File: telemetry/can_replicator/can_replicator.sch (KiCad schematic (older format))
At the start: 25 parts, among them J1 CONN_02X03, U1 MCP2561-E_SN, U2 ATMEGA16M1, Y1 Crystal_SMD

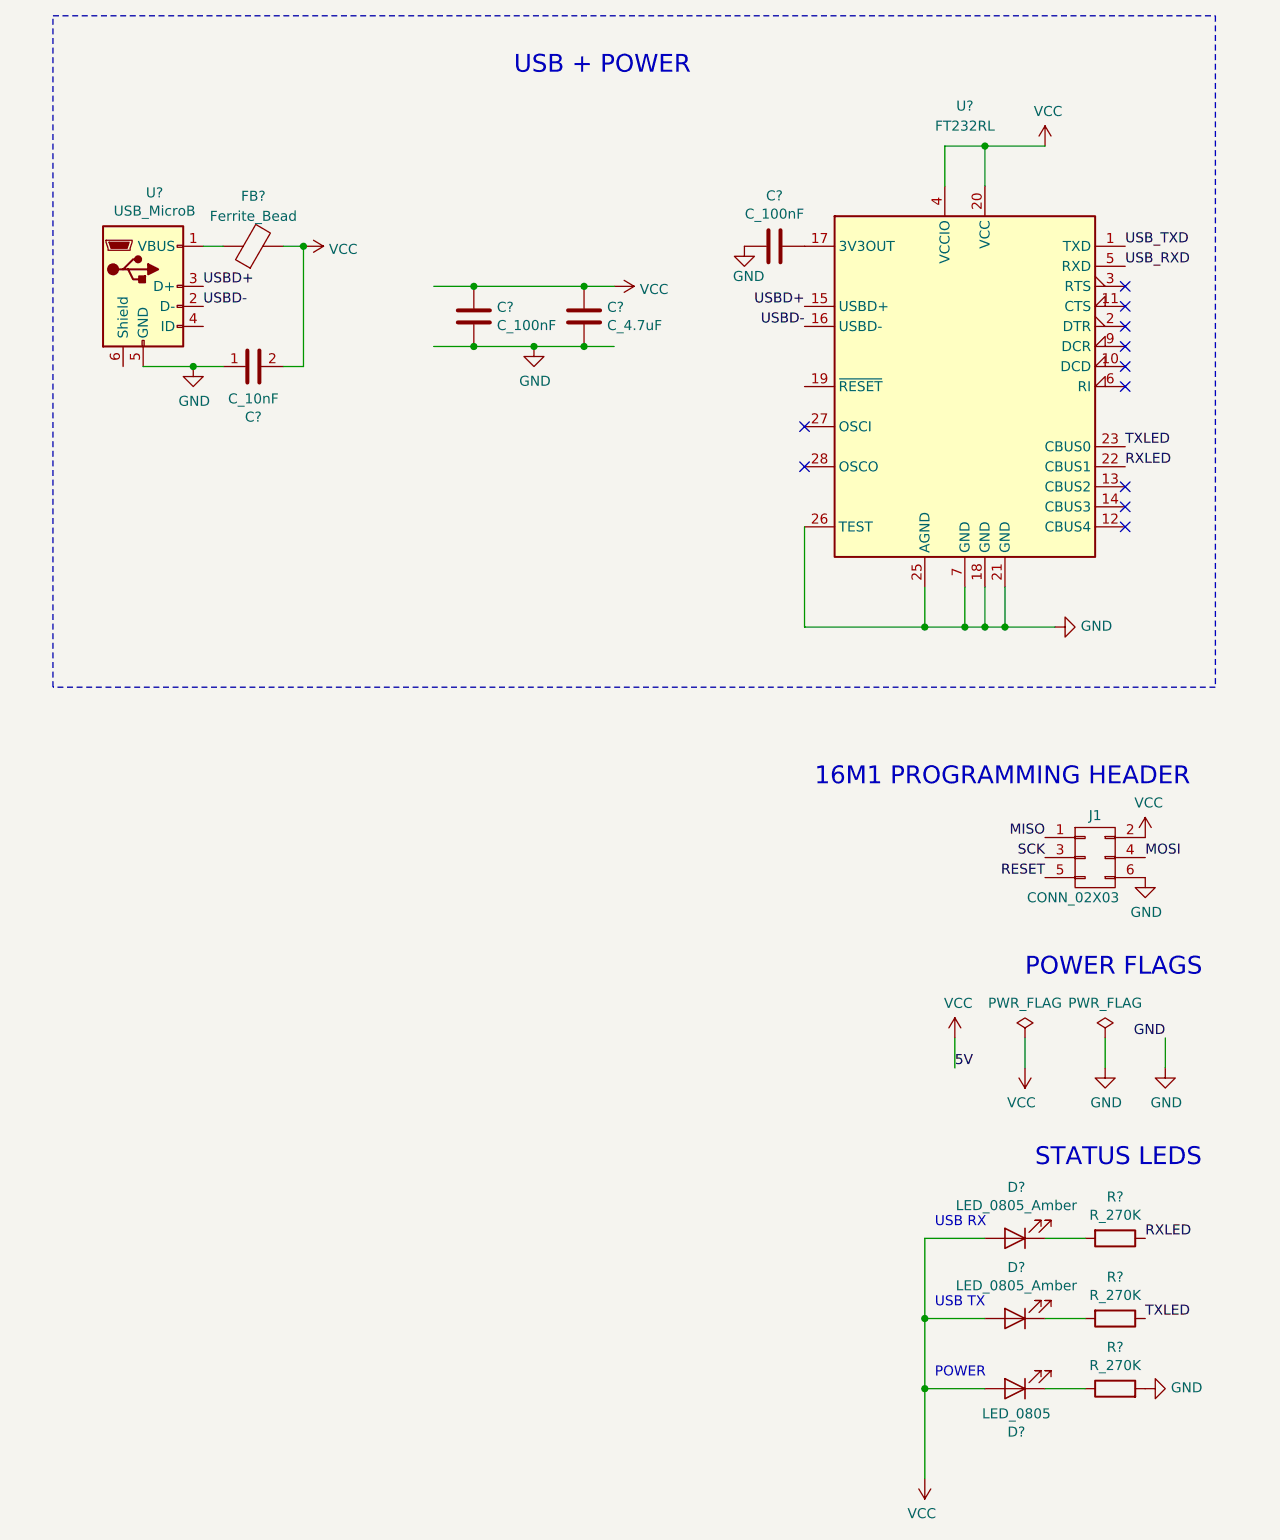
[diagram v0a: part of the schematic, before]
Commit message: fix: GND down, VCC up
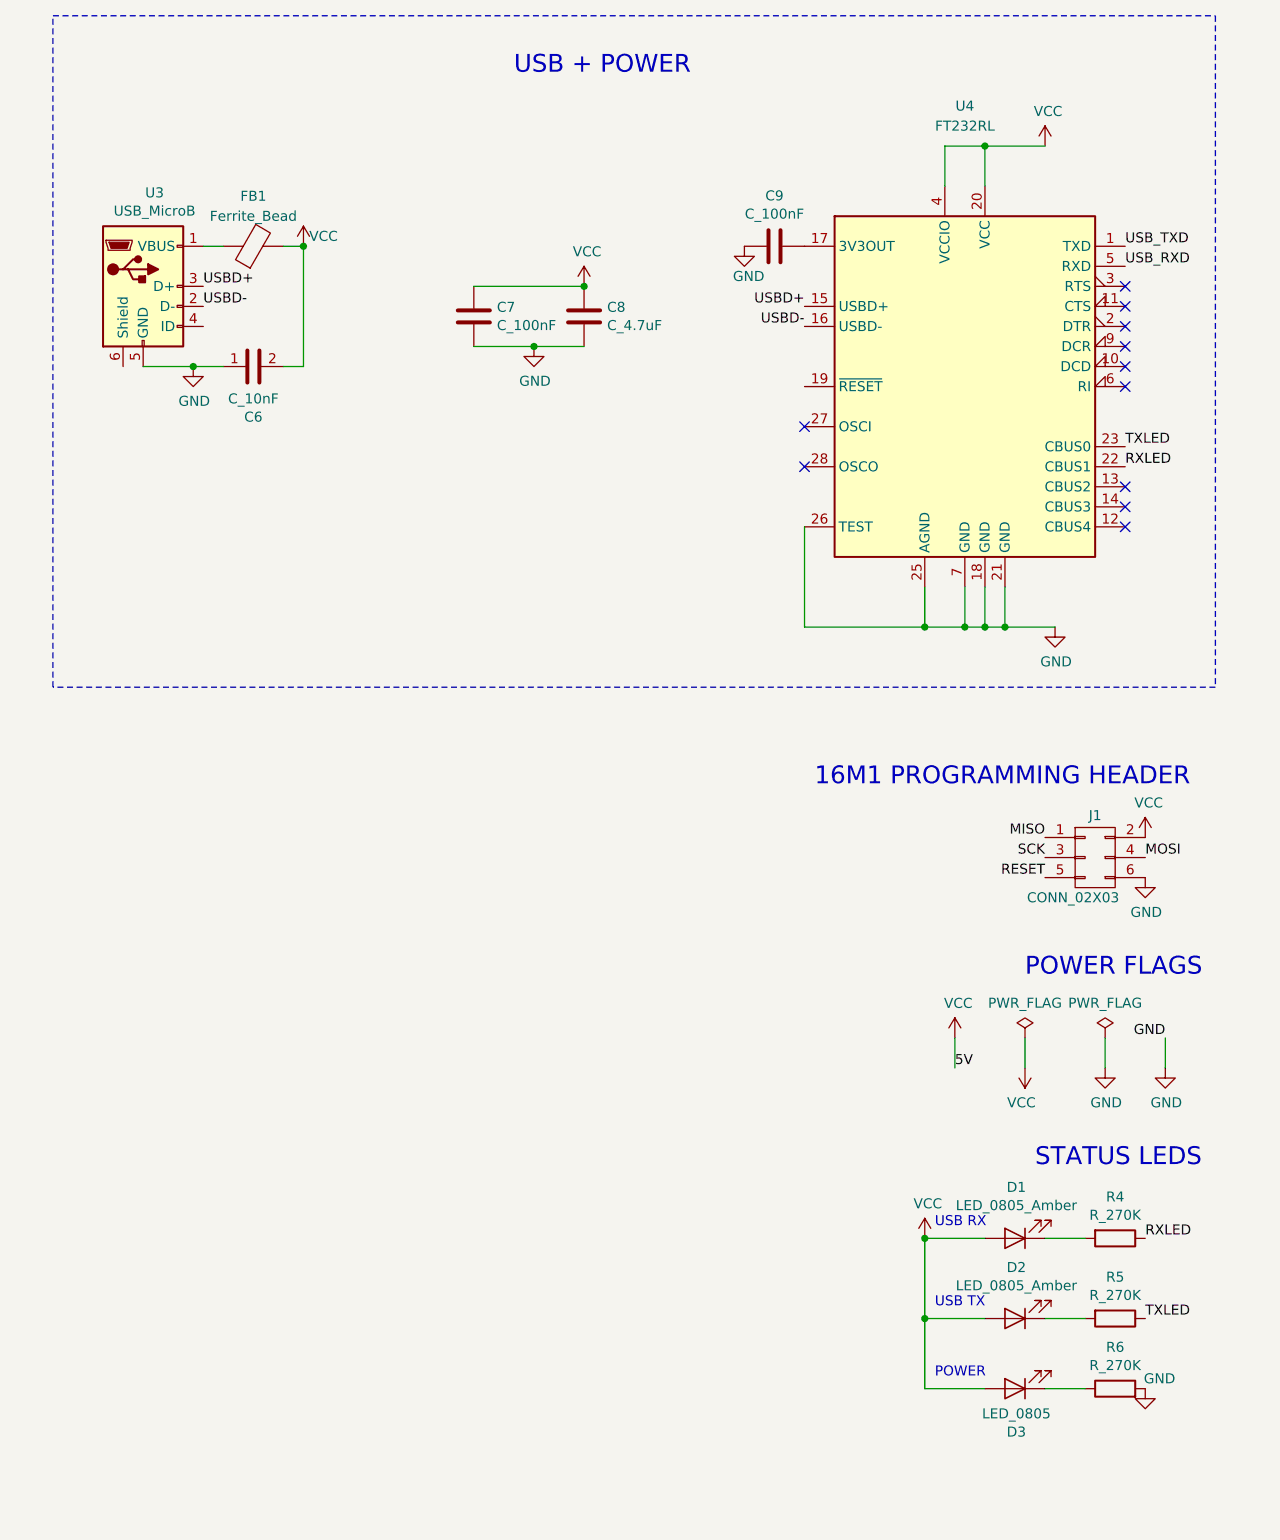
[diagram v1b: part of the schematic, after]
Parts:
- gave numbers to parts that had none: 13
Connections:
- wire segments 73 -> 68
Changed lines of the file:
@@
 Connection ~ 14800 3700
 $Comp
-L power:GND #PWR0101
-U 1 1 5FABE223
-P 15450 3700
-F 0 "#PWR0101" H 15450 3450 50  0001 C CNN
-F 1 "GND" V 15455 3572 50  0000 R CNN
-F 2 "" H 15450 3700 50  0001 C CNN
-F 3 "" H 15450 3700 50  0001 C CNN
-	1    15450 3700
-	0    -1   -1   0
-$EndComp
-$Comp
-L formula:FT232RL U?
+L formula:FT232RL U4
 U 1 1 5FA978AD
 P 15000 2500
-F 0 "U?" H 15000 3900 50  0000 C CNN
+F 0 "U4" H 15000 3900 50  0000 C CNN
 F 1 "FT232RL" H 15000 3800 50  0000 C CNN
 F 2 "Package_SO:SSOP-28_5.3x10.2mm_P0.65mm" H 16100 1600 50  0001 C CNN
@@
 $EndComp
 $Comp
-L formula:C_100nF C?
+L formula:C_100nF C9
 U 1 1 5FAC0003
 P 14050 1800
-F 0 "C?" V 13798 1800 50  0000 C CNN
+F 0 "C9" V 13798 1800 50  0000 C CNN
 F 1 "C_100nF" V 13889 1800 50  0000 C CNN
 F 2 "footprints:C_0603_1608Metric" H 14088 1650 50  0001 C CNN
@@
 	10900 2400 11150 2400
 $Comp
-L formula:USB_MicroB U?
+L formula:USB_MicroB U3
 U 1 1 5FA94609
 P 10900 2000
-F 0 "U?" H 10957 2467 50  0000 C CNN
+F 0 "U3" H 10957 2467 50  0000 C CNN
 F 1 "USB_MicroB" H 10957 2376 50  0000 C CNN
 F 2 "Connectors_USB:USB_Micro-B_Molex-105017-0001" H 10850 2350 50  0001 C CNN
@@
 	11700 2400 11600 2400
 $Comp
-L formula:C_10nF C?
+L formula:C_10nF C6
 U 1 1 5FAF39CA
 P 11450 2400
-F 0 "C?" V 11198 2400 50  0000 C CNN
+F 0 "C6" V 11198 2400 50  0000 C CNN
 F 1 "C_10nF" V 11289 2400 50  0000 C CNN
 F 2 "footprints:C_0805_OEM" H 11250 2400 50  0001 C CNN
@@
 	11200 1800 11300 1800
 $Comp
-L Device:Ferrite_Bead FB?
+L Device:Ferrite_Bead FB1
 U 1 1 5FAF9058
 P 11450 1800
-F 0 "FB?" V 11700 1800 50  0000 C CNN
+F 0 "FB1" V 11700 1800 50  0000 C CNN
 F 1 "Ferrite_Bead" V 11600 1800 50  0000 C CNN
 F 2 "" V 11380 1800 50  0001 C CNN
@@
 Wire Wire Line
 	11600 1800 11700 1800
-$Comp
-L power:VCC #PWR0105
-U 1 1 5FAFC426
-P 11700 1800
-F 0 "#PWR0105" H 11700 1650 50  0001 C CNN
-F 1 "VCC" V 11715 1927 50  0000 L CNN
-F 2 "" H 11700 1800 50  0001 C CNN
-F 3 "" H 11700 1800 50  0001 C CNN
-	1    11700 1800
-	0    1    1    0
-$EndComp
 Connection ~ 11700 1800
-Wire Wire Line
-	12350 2000 12550 2000
-Wire Wire Line
-	12350 2300 12550 2300
-$Comp
-L power:VCC #PWR0106
-U 1 1 5FB299EF
-P 13250 2000
-F 0 "#PWR0106" H 13250 1850 50  0001 C CNN
-F 1 "VCC" V 13265 2128 50  0000 L CNN
-F 2 "" H 13250 2000 50  0001 C CNN
-F 3 "" H 13250 2000 50  0001 C CNN
-	1    13250 2000
-	0    1    1    0
-$EndComp
 $Comp
 L power:GND #PWR0107
@@
 	12850 2300 13100 2300
 $Comp
-L formula:C_100nF C?
+L formula:C_100nF C7
 U 1 1 5FB2B96B
 P 12550 2150
-F 0 "C?" H 12665 2196 50  0000 L CNN
+F 0 "C7" H 12665 2196 50  0000 L CNN
 F 1 "C_100nF" H 12665 2105 50  0000 L CNN
 F 2 "footprints:C_0603_1608Metric" H 12588 2000 50  0001 C CNN
@@
 	1    0    0    -1
 $EndComp
-Connection ~ 12550 2000
 Wire Wire Line
 	12550 2000 13100 2000
 $Comp
-L formula:C_4.7uF C?
+L formula:C_4.7uF C8
 U 1 1 5FB2C8CC
 P 13100 2150
-F 0 "C?" H 13215 2196 50  0000 L CNN
+F 0 "C8" H 13215 2196 50  0000 L CNN
 F 1 "C_4.7uF" H 13215 2105 50  0000 L CNN
 F 2 "footprints:C_0603_1608Metric" H 13138 2000 50  0001 C CNN
@@
 	1    0    0    -1
 $EndComp
-Connection ~ 13100 2000
-Wire Wire Line
-	13100 2000 13250 2000
-Connection ~ 12550 2300
 Wire Wire Line
 	12550 2300 12850 2300
-Connection ~ 13100 2300
-Wire Wire Line
-	13100 2300 13250 2300
-$Comp
-L formula:LED_0805 D?
+$Comp
+L formula:LED_0805 D3
 U 1 1 5FB4670F
 P 15250 7500
-F 0 "D?" H 15243 7716 50  0000 C CNN
+F 0 "D3" H 15243 7716 50  0000 C CNN
 F 1 "LED_0805" H 15243 7625 50  0000 C CNN
 F 2 "footprints:LED_0805_OEM" H 15150 7500 50  0001 C CNN
@@
 	-1   0    0    1
 $EndComp
-$Comp
-L power:VCC #PWR?
-U 1 1 5FB4B1C8
-P 14800 7950
-F 0 "#PWR?" H 14800 7800 50  0001 C CNN
-F 1 "VCC" H 14815 8123 50  0000 C CNN
-F 2 "" H 14800 7950 50  0001 C CNN
-F 3 "" H 14800 7950 50  0001 C CNN
-	1    14800 7950
-	-1   0    0    1
-$EndComp
 Text Notes 14850 7450 0    50   ~ 0
 POWER
 Wire Wire Line
-	14800 7950 14800 7500
-Wire Wire Line
 	14800 7500 15100 7500
 $Comp
-L formula:R_270K R?
+L formula:R_270K R6
 U 1 1 5FB531FD
 P 15750 7500
-F 0 "R?" V 15957 7500 50  0000 C CNN
+F 0 "R6" V 15957 7500 50  0000 C CNN
 F 1 "R_270K" V 15866 7500 50  0000 C CNN
 F 2 "footprints:R_0805_OEM" V 15680 7500 50  0001 C CNN
@@
 $EndComp
 $Comp
-L power:GND #PWR?
-U 1 1 5FB5662E
-P 15900 7500
-F 0 "#PWR?" H 15900 7250 50  0001 C CNN
-F 1 "GND" V 15905 7372 50  0000 R CNN
-F 2 "" H 15900 7500 50  0001 C CNN
-F 3 "" H 15900 7500 50  0001 C CNN
-	1    15900 7500
-	0    -1   -1   0
-$EndComp
-$Comp
-L formula:LED_0805_Amber D?
+L formula:LED_0805_Amber D2
 U 1 1 5FB574C3
 P 15250 7150
-F 0 "D?" H 15243 6895 50  0000 C CNN
+F 0 "D2" H 15243 6895 50  0000 C CNN
 F 1 "LED_0805_Amber" H 15243 6986 50  0000 C CNN
 F 2 "footprints:LED_0805_OEM" H 15150 7150 50  0001 C CNN
@@
 $EndComp
 $Comp
-L formula:LED_0805_Amber D?
+L formula:LED_0805_Amber D1
 U 1 1 5FB5A256
 P 15250 6750
-F 0 "D?" H 15243 6495 50  0000 C CNN
+F 0 "D1" H 15243 6495 50  0000 C CNN
 F 1 "LED_0805_Amber" H 15243 6586 50  0000 C CNN
 F 2 "footprints:LED_0805_OEM" H 15150 6750 50  0001 C CNN
@@
 $EndComp
 $Comp
-L formula:R_270K R?
+L formula:R_270K R5
 U 1 1 5FB5AAD5
 P 15750 7150
-F 0 "R?" V 15543 7150 50  0000 C CNN
+F 0 "R5" V 15543 7150 50  0000 C CNN
 F 1 "R_270K" V 15634 7150 50  0000 C CNN
 F 2 "footprints:R_0805_OEM" V 15680 7150 50  0001 C CNN
@@
 $EndComp
 $Comp
-L formula:R_270K R?
+L formula:R_270K R4
 U 1 1 5FB5BC61
 P 15750 6750
-F 0 "R?" V 15543 6750 50  0000 C CNN
+F 0 "R4" V 15543 6750 50  0000 C CNN
 F 1 "R_270K" V 15634 6750 50  0000 C CNN
 F 2 "footprints:R_0805_OEM" V 15680 6750 50  0001 C CNN
@@
 Text Label 15800 2900 0    50   ~ 0
 RXLED
-Connection ~ 14800 7500
 Wire Wire Line
 	14800 7150 14800 7500
@@
 Wire Notes Line
 	6450 2650 6450 650
+$Comp
+L power:VCC #PWR?
+U 1 1 5FB3615E
+P 11700 1800
+F 0 "#PWR?" H 11700 1650 50  0001 C CNN
+F 1 "VCC" H 11800 1850 50  0000 C CNN
+F 2 "" H 11700 1800 50  0001 C CNN
+F 3 "" H 11700 1800 50  0001 C CNN
+	1    11700 1800
+	1    0    0    -1
+$EndComp
+$Comp
+L power:VCC #PWR?
+U 1 1 5FB37814
+P 13100 2000
+F 0 "#PWR?" H 13100 1850 50  0001 C CNN
+F 1 "VCC" H 13115 2173 50  0000 C CNN
+F 2 "" H 13100 2000 50  0001 C CNN
+F 3 "" H 13100 2000 50  0001 C CNN
+	1    13100 2000
+	1    0    0    -1
+$EndComp
+Connection ~ 13100 2000
+$Comp
+L power:GND #PWR?
+U 1 1 5FB3808B
+P 15450 3700
+F 0 "#PWR?" H 15450 3450 50  0001 C CNN
+F 1 "GND" H 15455 3527 50  0000 C CNN
+F 2 "" H 15450 3700 50  0001 C CNN
+F 3 "" H 15450 3700 50  0001 C CNN
+	1    15450 3700
+	1    0    0    -1
+$EndComp
+$Comp
+L power:GND #PWR0110
+U 1 1 5FB5662E
+P 15900 7500
+F 0 "#PWR0110" H 15900 7250 50  0001 C CNN
+F 1 "GND" H 16050 7550 50  0000 R CNN
+F 2 "" H 15900 7500 50  0001 C CNN
+F 3 "" H 15900 7500 50  0001 C CNN
+	1    15900 7500
+	1    0    0    -1
+$EndComp
+$Comp
+L power:VCC #PWR?
+U 1 1 5FB3A4ED
+P 14800 6750
+F 0 "#PWR?" H 14800 6600 50  0001 C CNN
+F 1 "VCC" H 14815 6923 50  0000 C CNN
+F 2 "" H 14800 6750 50  0001 C CNN
+F 3 "" H 14800 6750 50  0001 C CNN
+	1    14800 6750
+	1    0    0    -1
+$EndComp
+Connection ~ 14800 6750
 $EndSCHEMATC

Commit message: fix: replace resistor after tranciever with DNP 120ohm
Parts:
- removed R2: R_200, footprints:R_0805_OEM, symbol template-rescue:R_200-formula
- added R?: R_120_DNP, footprints:R_0805_OEM, symbol formula:R_120_DNP
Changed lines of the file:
@@
 	0    1    1    0
-$EndComp
-$Comp
-L template-rescue:R_200-formula R2
-U 1 1 5D5FB79E
-P 8200 1950
-F 0 "R2" V 8290 1900 50  0000 L CNN
-F 1 "R_200" V 8110 1830 50  0000 L CNN
-F 2 "footprints:R_0805_OEM" H 8130 1950 50  0001 C CNN
-F 3 "https://www.seielect.com/Catalog/SEI-RMCF_RMCP.pdf" H 8280 1950 50  0001 C CNN
-F 4 "DK" H 8200 1950 60  0001 C CNN "MFN"
-F 5 "RMCF0805JT200RCT-ND" H 8200 1950 60  0001 C CNN "MPN"
-F 6 "https://www.digikey.com/products/en?keywords=RMCF0805JT200RCT-ND" H 8680 2350 60  0001 C CNN "PurchasingLink"
-	1    8200 1950
-	1    0    0    -1
 $EndComp
 NoConn ~ 7900 1950
@@
 	8000 1850 8000 1800
 Wire Wire Line
-	8000 1800 8200 1800
-Connection ~ 8200 1800
-Wire Wire Line
-	8200 1800 8350 1800
-Wire Wire Line
 	8000 2050 8000 2100
-Wire Wire Line
-	8000 2100 8200 2100
-Connection ~ 8200 2100
-Wire Wire Line
-	8200 2100 8350 2100
 Wire Wire Line
 	14950 5750 14950 5900
@@
 $EndComp
 Connection ~ 14800 6750
+Wire Wire Line
+	8000 1800 8200 1800
+Wire Wire Line
+	8000 2100 8200 2100
+$Comp
+L formula:R_120_DNP R?
+U 1 1 5FB3CE18
+P 8200 1950
+F 0 "R?" H 8050 1950 50  0000 L CNN
+F 1 "R_120_DNP" H 8250 1950 50  0000 L CNN
+F 2 "footprints:R_0805_OEM" H 7000 2100 50  0001 L CNN
+F 3 "https://www.mouser.com/datasheet/2/315/AOA0000C304-1149620.pdf" H 7000 2400 50  0001 L CNN
+F 4 "DK" H 8200 1950 60  0001 C CNN "MFN"
+F 5 "667-ERJ-6ENF1200V" H 7000 2200 60  0001 L CNN "MPN"
+F 6 "https://www.mouser.com/ProductDetail/Panasonic-Industrial-Devices/ERJ-6ENF1200V?qs=sGAEpiMZZMvdGkrng054t8AJgcdMkx7x%252bFQnctTMUmU%3d" H 7000 2300 60  0001 L CNN "PurchasingLink"
+	1    8200 1950
+	1    0    0    -1
+$EndComp
+Connection ~ 8200 1800
+Wire Wire Line
+	8200 1800 8350 1800
+Connection ~ 8200 2100
+Wire Wire Line
+	8200 2100 8350 2100
 $EndSCHEMATC
